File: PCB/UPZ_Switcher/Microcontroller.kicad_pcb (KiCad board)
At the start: 2 copper layers, 17 parts, among them IC1 MAX232ECPE+, J1 5747844-6, SW1 SW_DIP_x04, SW2 SW_DIP_x04

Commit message: updated phantom design + MCU board
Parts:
- added C19: 1uF, Capacitor_THT:CP_Radial_D5.0mm_P2.50mm, F.Cu at (188.5, 143.6)
- added C20: 1uF, Capacitor_THT:CP_Radial_D5.0mm_P2.50mm, F.Cu at (194.5, 143.5)
- added C21: 1uF, Capacitor_THT:CP_Radial_D5.0mm_P2.50mm, F.Cu at (200.8, 143.5)
- added C22: 1uF, Capacitor_THT:CP_Radial_D5.0mm_P2.50mm, F.Cu at (182.3, 143.6)
- added J2: TO RELAY, BVKSound:71918-110LF, F.Cu at (66.2, 146.4)
- added J3: FROM PREVIOUS, Connector_Dsub:DSUB-9_Female_Horizontal_P2.77x2.84mm_EdgePinOffset4.94mm_Housed_MountingHolesOffset7.48mm, F.Cu at (118.7, 112.6)
- added J4: TO NEXT, Connector_Dsub:DSUB-9_Male_Horizontal_P2.77x2.84mm_EdgePinOffset4.94mm_Housed_MountingHolesOffset7.48mm, F.Cu at (200.9, 112.6)
- J1: value 5747844-6 -> FROM PSU; footprint BVKSound:57478446 -> BVKSound:71918-110LF
- moved R2 115.5 mm to (70.4, 122.7)
- moved R4 104.3 mm to (77.3, 122.7)
- moved R7 103.3 mm to (77.4, 115.3)
- moved R5 98.9 mm to (77.3, 111.7)
- moved R1 98.0 mm to (70.3, 108.2)
- moved IC1 95.4 mm to (197.4, 131.5), turned to 90 degrees
- moved XA1 92.1 mm to (119.2, 148.6)
- moved J1 78.1 mm to (41.6, 122.6), turned to 270 degrees
- moved SW2 71.1 mm to (84.2, 125.8)
- moved R47 68.1 mm to (144.9, 124.0), turned to 270 degrees
- moved R46 66.5 mm to (148.7, 124.0), turned to 270 degrees
- moved R6 66.4 mm to (77.4, 126.2)
- moved SW1 65.3 mm to (84.2, 109.4)
- moved R3 59.1 mm to (77.4, 108.2)
- moved R8 53.7 mm to (77.4, 129.8)
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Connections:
- J1 pad 2: Net-(IC1-Pad14) -> Net-(J1-Pad2)
- J1 pad 3: Net-(IC1-Pad13) -> /5V
- J1 pad 6: Net-(J1-Pad4) -> Net-(J1-Pad6)
- J1 pad 8: Net-(J1-Pad7) -> Net-(J1-Pad8)
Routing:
- net GND: track 0.00 -> 400.7 mm, vias 0 -> 3
- net /5V: track 0.00 -> 284.6 mm, vias 0 -> 4
- net /I2C_SCK: track 0.00 -> 137.1 mm, vias 0 -> 4
- net /I2C_SDA: track 0.00 -> 134.8 mm, vias 0 -> 4
- net Net-(R1-Pad2): track 0.00 -> 111.4 mm
- net Net-(IC1-Pad14): track 0.00 -> 91.2 mm, vias 0 -> 2
- net Net-(IC1-Pad13): track 0.00 -> 90.3 mm, vias 0 -> 1
- net Net-(IC1-Pad11): track 0.00 -> 82.5 mm
- net Net-(R10-Pad1): track 0.00 -> 77.5 mm
- net Net-(IC1-Pad12): track 0.00 -> 75.8 mm
- net Net-(J1-Pad8): track 0.00 -> 68.8 mm, vias 0 -> 2
- net Net-(J1-Pad6): track 0.00 -> 67.2 mm, vias 0 -> 2
- net Net-(J1-Pad10): track 0.00 -> 53.6 mm
- net Net-(J1-Pad9): track 0.00 -> 52.0 mm, vias 0 -> 2
- net Net-(J1-Pad7): track 0.00 -> 44.8 mm
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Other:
- board outline added: 194 x 48 mm
- board text added: "Input Switch ID"
- board text added: "Output Switch ID"

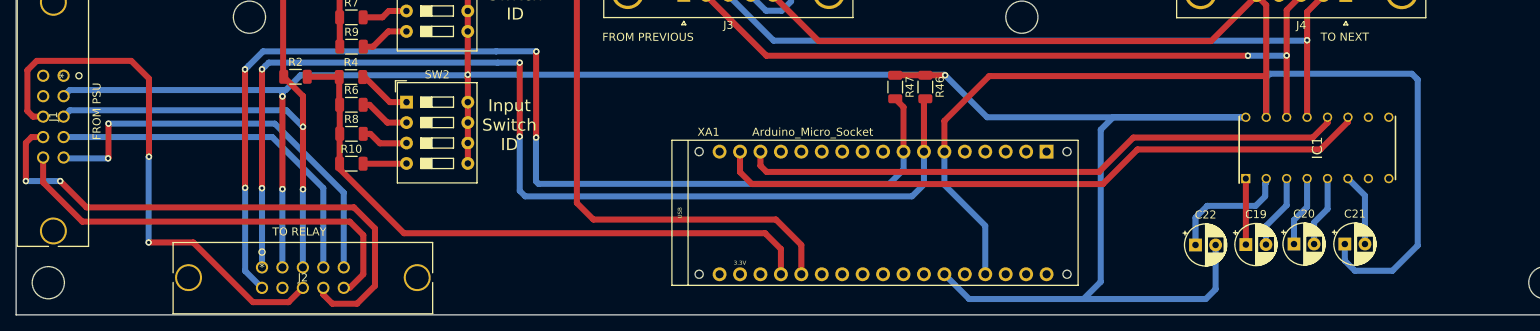
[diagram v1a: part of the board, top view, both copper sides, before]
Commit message: update on power supply
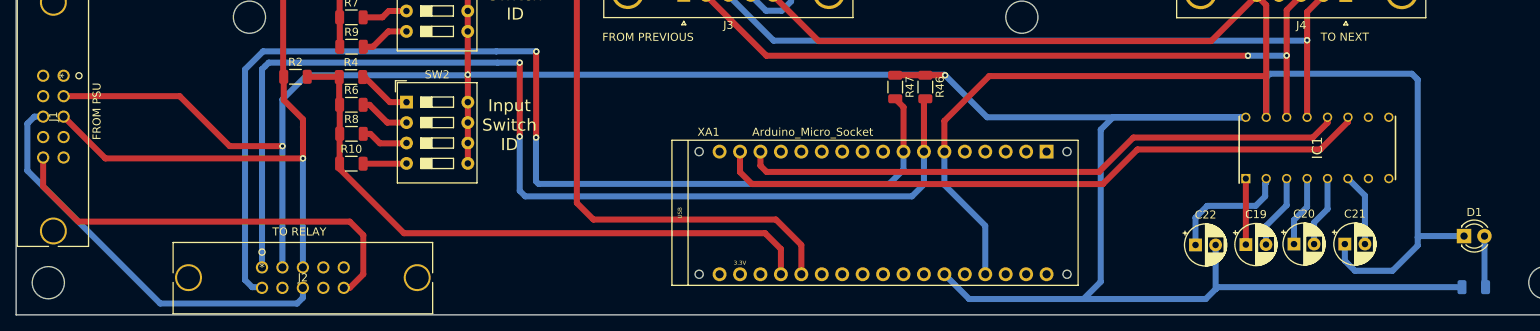
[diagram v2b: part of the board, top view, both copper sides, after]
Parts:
- added D1: LED, LED_THT:LED_D3.0mm, F.Cu at (215.6, 142.5)
- added R11: 100, Resistor_SMD:R_1206_3216Metric, B.Cu at (216.9, 148.8)
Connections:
- J2 pad 7: Net-(J1-Pad7) -> Net-(J2-Pad7)
- J2 pad 8: Net-(J1-Pad8) -> Net-(J2-Pad8)
- J2 pad 9: Net-(J1-Pad9) -> Net-(J2-Pad9)
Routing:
- net Net-(J1-Pad8): track 68.8 -> 0.00 mm, vias 2 -> 0
- net Net-(J1-Pad9): track 52.0 -> 0.16 mm, vias 2 -> 0
- net Net-(J1-Pad7): track 44.8 -> 0.00 mm
- net /5V: track 284.6 -> 316.5 mm, vias 4 -> 3
- net Net-(J1-Pad6): track 67.2 -> 50.8 mm, vias 2 -> 0
- net GND: track 400.7 -> 407.5 mm, vias 3 -> 2
- net Net-(D1-Pad2): track 0.00 -> 6.40 mm
- net /I2C_SCK: track 137.1 -> 137.8 mm, vias 4 -> 2
- net /I2C_SDA: vias 4 -> 2

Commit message: final
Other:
- board text added: "UPZ Switcher MCU Board BVKSound 2021-03"
